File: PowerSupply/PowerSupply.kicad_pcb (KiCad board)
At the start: 2 copper layers, 21 parts, among them J1 AC+, J2 AC-, J3 POWER, U1 LM317_SOT-223, U2 LM337_SOT223

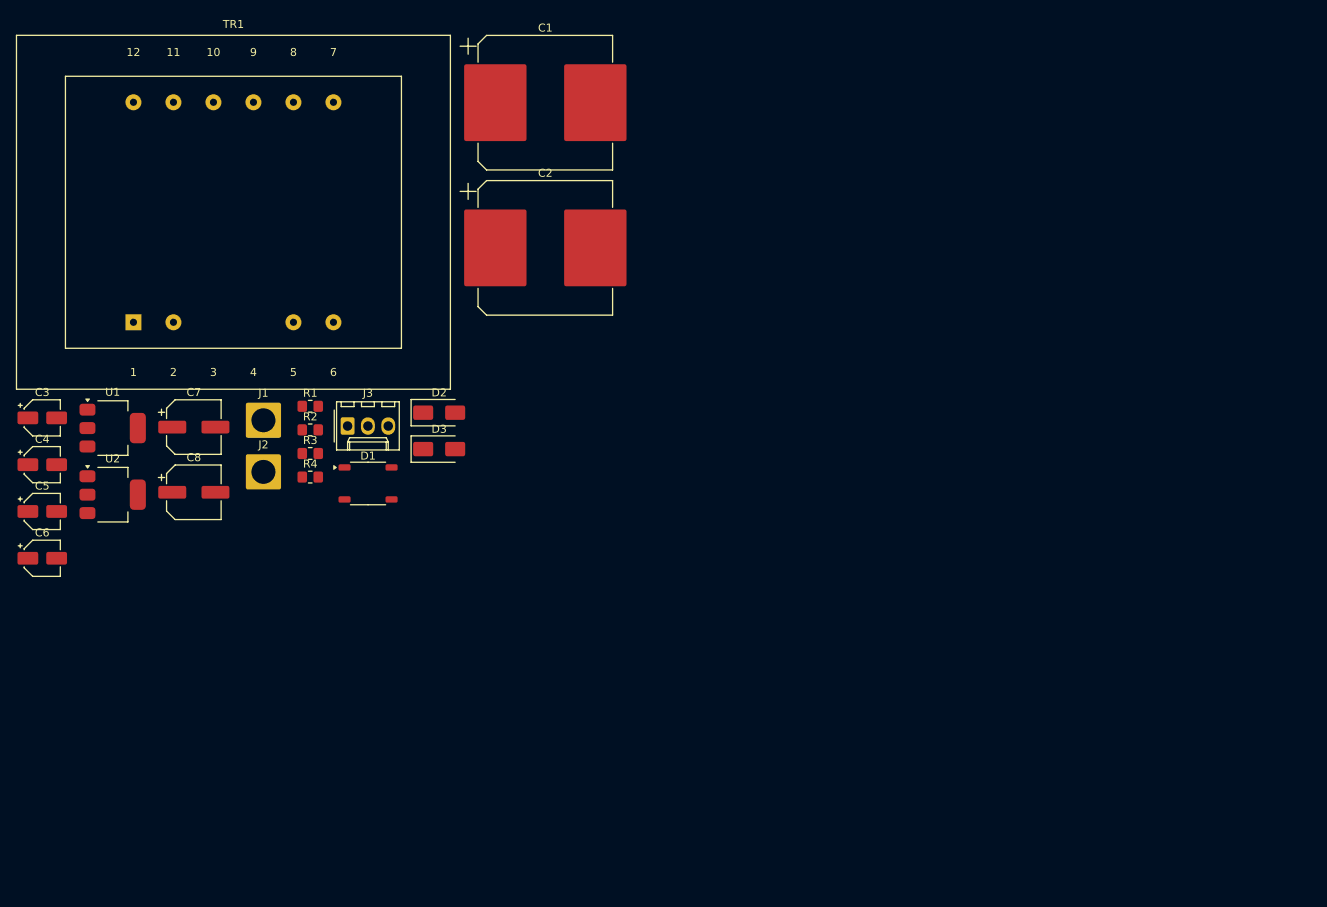
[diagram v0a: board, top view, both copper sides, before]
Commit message: Power Supply Board
Updated the power supply schematic.
Updated the power supply board.
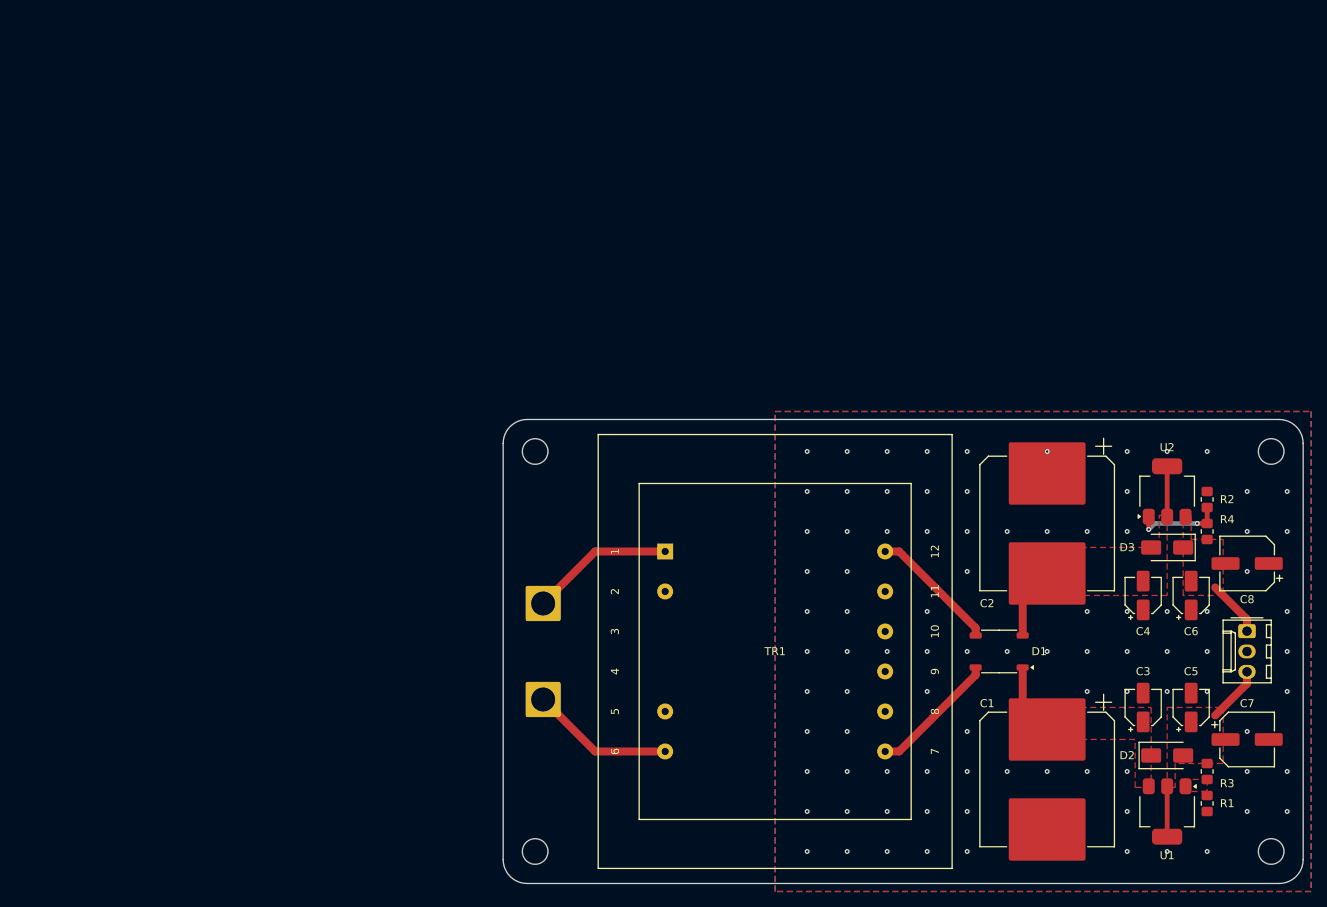
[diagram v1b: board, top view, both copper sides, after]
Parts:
- added H1: MountingHole, MountingHole:MountingHole_3.2mm_M3, F.Cu at (91.0, 75.0)
- added H2: MountingHole, MountingHole:MountingHole_3.2mm_M3, F.Cu at (183.0, 75.0)
- added H3: MountingHole, MountingHole:MountingHole_3.2mm_M3, F.Cu at (91.0, 125.0)
- added H4: MountingHole, MountingHole:MountingHole_3.2mm_M3, F.Cu at (183.0, 125.0)
- moved C5 145.7 mm to (173.0, 107.0), turned to 90 degrees
- moved C6 143.7 mm to (173.0, 93.0), turned to 90 degrees
- moved C3 142.3 mm to (167.0, 107.0), turned to 90 degrees
- moved U1 140.3 mm to (170.0, 120.0), turned to -90 degrees
- moved C4 138.6 mm to (167.0, 93.0), turned to 90 degrees
- moved C7 137.3 mm to (180.0, 111.0)
- moved C8 132.0 mm to (180.0, 89.0), turned to 180 degrees
- moved U2 131.8 mm to (170.0, 80.0), turned to 90 degrees
- moved R1 122.6 mm to (175.0, 119.0), turned to -90 degrees
- moved R3 119.0 mm to (175.0, 115.0), turned to 90 degrees
- moved J3 115.3 mm to (180.0, 97.5), turned to -90 degrees
- moved R2 112.5 mm to (175.0, 81.0), turned to -90 degrees
- moved R4 112.3 mm to (175.0, 85.0), turned to -90 degrees
- moved C1 105.3 mm to (155.0, 116.0), turned to -90 degrees
- moved D2 100.6 mm to (170.0, 113.0)
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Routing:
- net Net-(J2-Pin_1): track 0.00 -> 17.9 mm
- net Net-(J1-Pin_1): track 0.00 -> 17.9 mm
- net Net-(D1-Pad4): track 0.00 -> 16.0 mm
- net Net-(D1-Pad3): track 0.00 -> 16.0 mm
- net -15V: track 0.00 -> 15.1 mm
- net +12V: track 0.00 -> 13.4 mm
- net Net-(U2-ADJ): track 0.00 -> 11.2 mm, vias 0 -> 2
- net +15V: track 0.00 -> 8.82 mm
- net -12V: track 0.00 -> 7.11 mm
- net GND: vias 0 -> 92
- added copper zone on F.Cu, net +12V
- added copper zone on F.Cu, net +15V
- added copper zone on F.Cu, net -12V
- added copper zone on F.Cu, net -15V
- added copper zone on B.Cu, net GND
- added copper zone on F.Cu, net GND
- added copper zone on F.Cu, net Net-(U1-ADJ)
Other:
- board outline added: 100 x 58 mm

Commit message: Power Supply Board
Updated the power supply board design.
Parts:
- added G***: LOGO, Logos:Cat, F.Cu at (160.5, 100.0)
- J3: footprint Connector_Molex:Molex_KK-254_AE-6410-03A_1x03_P2.54mm_Vertical -> Custom_Parts:Molex_KK-254_1x03_P2.54mm_Vertical
- TR1: footprint Transformer_THT:Transformer_Breve_TEZ-44x52 -> Custom_Parts:TRANSFORMER_TEZ-44X52
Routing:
- net GND: vias 92 -> 69
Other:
- board text added: "+"
- board text added: "-"
- board text added: "AC+"
- board text added: "AC-"
- board text added: "G"
- board text added: "PD 08/25"
- board text added: "POWER"
- board text added: "POWER SUPPLY"
- board text added: "REV A"
- board text added: "VERSION 1.0"

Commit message: Board Designs
Updated the power supply board design.
Updated the preamplifier board design.
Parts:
- added G***: LOGO, Logos:PowerSupply, B.Cu at (161.4, 100.0)
- added G***: LOGO, Logos:HighVoltage, B.Cu at (117.1, 99.5)
